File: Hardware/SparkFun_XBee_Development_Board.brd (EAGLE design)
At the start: 45.7 x 63.5 mm, 150 parts, among them J4 QWIIC_RIGHT_ANGLE, Q2 3.1A/30V/105mΩ, U1 FSUSB30MUX_MSOP10, U2 AP63203, U3 ESD Diode, U4 MCP73831, U5 ESD Diode, U7 FT231XS

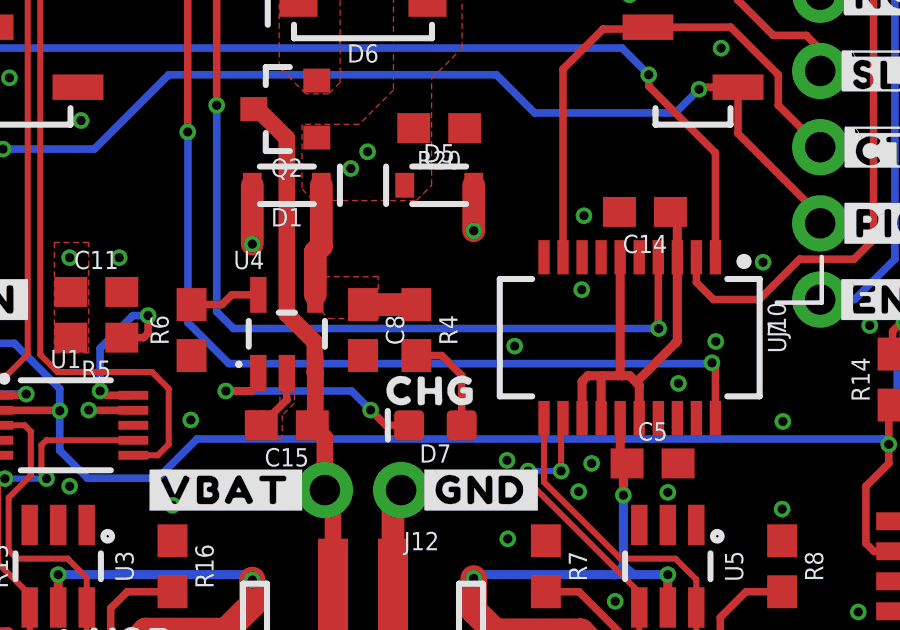
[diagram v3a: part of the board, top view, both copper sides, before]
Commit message: Moves ground pin nets to the bottom of the decoupling cap
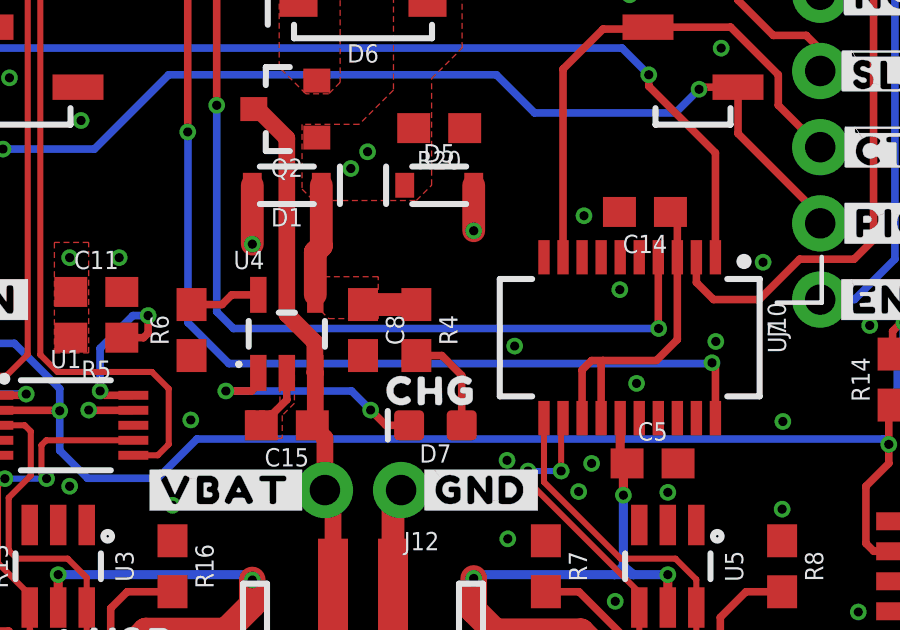
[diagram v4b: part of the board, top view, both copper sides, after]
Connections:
- net GND: now also U7.16, U7.6
- net N$18: no longer U7.16, U7.6
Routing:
- net N$18: track 16.3 -> 11.5 mm
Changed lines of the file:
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@@
 <via x="6.35" y="38.1" extent="1-16" drill="0.3048"/>
 <via x="6.35" y="40.64" extent="1-16" drill="0.3048"/>
-<contactref element="C14" pad="2"/>
 <contactref element="C5" pad="2"/>
 <via x="30.226" y="21.844" extent="1-16" drill="0.3048"/>
 <via x="27.9146" y="17.5006" extent="1-16" drill="0.3048"/>
-<via x="30.1498" y="19.3802" extent="1-16" drill="0.3048"/>
-<via x="33.3756" y="16.256" extent="1-16" drill="0.3048"/>
+<via x="31.4198" y="19.3802" extent="1-16" drill="0.3048"/>
+<via x="31.9786" y="16.256" extent="1-16" drill="0.3048"/>
 <via x="34.6202" y="17.653" extent="1-16" drill="0.3048"/>
 <via x="14.732" y="20.447" extent="1-16" drill="0.3048"/>
@@
 </polygon>
 <via x="36.195" y="20.2946" extent="1-16" drill="0.3048"/>
+<contactref element="U7" pad="6"/>
+<contactref element="C14" pad="2"/>
+<contactref element="U7" pad="16"/>
 </signal>
 <signal name="3.3V">
@@
 <via x="34.4932" y="16.9418" extent="1-16" drill="0.3048"/>
 <wire x1="34.4932" y1="16.9164" x2="34.4932" y2="16.9418" width="0.254" layer="16"/>
-<wire x1="34.4932" y1="16.9164" x2="18.3896" y2="16.9164" width="0.254" layer="16"/>
-<wire x1="18.3896" y1="16.9164" x2="17.0262" y2="18.2798" width="0.254" layer="16"/>
+<wire x1="17.0262" y1="18.2798" x2="18.3896" y2="16.9164" width="0.254" layer="16"/>
 <wire x1="17.018" y1="24.638" x2="17.0262" y2="24.6298" width="0.254" layer="16"/>
 <wire x1="17.0262" y1="24.6298" x2="17.0262" y2="18.2798" width="0.254" layer="16"/>
 <wire x1="13.565596875" y1="40.130003125" x2="10.160003125" y2="40.130003125" width="0.254" layer="1"/>
 <wire x1="10.160003125" y1="40.130003125" x2="10.16" y2="40.13" width="0.254" layer="1"/>
+<wire x1="18.3896" y1="16.9164" x2="34.4932" y2="16.9164" width="0.254" layer="16"/>
 </signal>
 <signal name="D12/SPI_POCI">
@@
 </signal>
 <signal name="N$18">
-<contactref element="U7" pad="16"/>
-<contactref element="C14" pad="1"/>
-<contactref element="U7" pad="6"/>
 <contactref element="U7" pad="14"/>
 <contactref element="U7" pad="3"/>
 <contactref element="U7" pad="13"/>
-<wire x1="32.0675" y1="15.1003" x2="32.0675" y2="15.24" width="0.3048" layer="1"/>
-<wire x1="30.353" y1="16.51" x2="30.861" y2="16.51" width="0.3048" layer="1"/>
-<wire x1="30.861" y1="16.51" x2="31.496" y2="16.51" width="0.3048" layer="1"/>
-<wire x1="31.496" y1="16.51" x2="31.75" y2="16.51" width="0.3048" layer="1"/>
-<wire x1="30.1625" y1="15.1003" x2="30.1625" y2="16.3195" width="0.3048" layer="1"/>
-<wire x1="30.1625" y1="16.3195" x2="30.353" y2="16.51" width="0.3048" layer="1"/>
-<wire x1="30.7975" y1="15.1003" x2="30.7975" y2="16.4465" width="0.3048" layer="1"/>
-<wire x1="30.7975" y1="16.4465" x2="30.861" y2="16.51" width="0.3048" layer="1"/>
-<wire x1="33.3375" y1="20.4597" x2="33.3375" y2="17.6657" width="0.3048" layer="1"/>
-<wire x1="33.3375" y1="17.6657" x2="33.274" y2="17.6022" width="0.3048" layer="1"/>
-<wire x1="33.274" y1="17.6022" x2="33.274" y2="17.59933125" width="0.3048" layer="1"/>
-<wire x1="31.967334375" y1="16.292665625" x2="33.274" y2="17.59933125" width="0.3048" layer="1"/>
-<wire x1="31.75" y1="16.51" x2="31.967334375" y2="16.292665625" width="0.3048" layer="1"/>
-<wire x1="31.4325" y1="20.4597" x2="31.4325" y2="16.5735" width="0.3048" layer="1"/>
-<wire x1="31.4325" y1="16.5735" x2="31.496" y2="16.51" width="0.3048" layer="1"/>
-<wire x1="32.0675" y1="15.1003" x2="32.0675" y2="16.1925" width="0.3048" layer="1"/>
-<wire x1="32.0675" y1="16.1925" x2="31.967334375" y2="16.292665625" width="0.3048" layer="1"/>
-<wire x1="33.3375" y1="20.4597" x2="33.3375" y2="21.7415" width="0.3048" layer="1"/>
-<wire x1="33.3375" y1="21.7415" x2="33.108" y2="21.971" width="0.3048" layer="1"/>
+<contactref element="C14" pad="1"/>
+<wire x1="30.1625" y1="15.1003" x2="30.1625" y2="16.7005" width="0.254" layer="1"/>
+<wire x1="30.48" y1="17.018" x2="30.861" y2="17.018" width="0.254" layer="1"/>
+<wire x1="30.861" y1="17.018" x2="32.639" y2="17.018" width="0.254" layer="1"/>
+<wire x1="33.3375" y1="17.7165" x2="33.3375" y2="20.4597" width="0.254" layer="1"/>
+<wire x1="30.1625" y1="16.7005" x2="30.48" y2="17.018" width="0.254" layer="1"/>
+<wire x1="32.639" y1="17.018" x2="33.3375" y2="17.7165" width="0.254" layer="1"/>
+<wire x1="30.7975" y1="16.9545" x2="30.861" y2="17.018" width="0.254" layer="1"/>
+<wire x1="30.7975" y1="15.1003" x2="30.7975" y2="16.9545" width="0.254" layer="1"/>
+<wire x1="33.108" y1="21.971" x2="33.3375" y2="21.7415" width="0.254" layer="1"/>
+<wire x1="33.3375" y1="21.7415" x2="33.3375" y2="20.4597" width="0.254" layer="1"/>
 </signal>
 </signals>
